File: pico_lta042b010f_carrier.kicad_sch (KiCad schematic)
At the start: 23 parts, among them J1 LTA042B010F_FFC36, J2 5V INPUT, J3 13V8 OUT, U1 RaspberryPi_Pico_2W, U3 MC34063AD

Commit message: chore(kicad): checkpoint before PCB artwork
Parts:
- C11: value 10u 25V -> 10uF 50V; AkizukiCode (none) -> 117897; MPN (none) -> 50PX10MEFC5X11; Manufacturer (none) -> Rubycon; SelectionNote (none) -> 10uF 50V 105C; radial through-hole; positive terminal to GND; SourceURL (none) -> https://akizukidenshi.com/catalog/g/g117897/; Supplier (none) -> Akizuki Denshi
- C6: value 220u 16V -> 220uF 35V; footprint Capacitor_THT:CP_Radial_D5.0mm_P2.00mm -> Capacitor_THT:CP_Radial_D8.0mm_P3.50mm; AkizukiCode (none) -> 111758; MPN (none) -> 35ZLH220MEFCCT8X11.5; Manufacturer (none) -> Rubycon; SelectionNote (none) -> 220uF 35V; linked item sold out; current equivalent candida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; SourceURL (none) -> https://akizukidenshi.com/catalog/g/g111758/; Supplier (none) -> Akizuki Denshi
- C7: value 470p -> 470pF 50V C0G; footprint Capacitor_SMD:C_0805_2012Metric -> Capacitor_THT:C_Disc_D5.0mm_W2.5mm_P2.50mm; AkizukiCode (none) -> 131236; MPN (none) -> RDE5C1H471J0P1H03B; Manufacturer (none) -> Murata; SelectionNote (none) -> 470pF 50V C0G +/-5%; radial through-hole; 2.5mm pitch; SourceURL (none) -> https://akizukidenshi.com/catalog/g/g131236/; Supplier (none) -> Akizuki Denshi
- C8: value 47u 25V -> 47uF 35V; AkizukiCode (none) -> 117887; MPN (none) -> 35PX47MEFC5X11; Manufacturer (none) -> Rubycon; SelectionNote (none) -> 47uF 35V; radial through-hole; SourceURL (none) -> https://akizukidenshi.com/catalog/g/g117887/; Supplier (none) -> Akizuki Denshi
- C9: value 10u 25V -> 10uF 50V; AkizukiCode (none) -> 117897; MPN (none) -> 50PX10MEFC5X11; Manufacturer (none) -> Rubycon; SelectionNote (none) -> 10uF 50V 105C; radial through-hole; SourceURL (none) -> https://akizukidenshi.com/catalog/g/g117897/; Supplier (none) -> Akizuki Denshi
- D4, D6, D7: footprint Diode_SMD:D_SMA -> Diode_THT:D_DO-41_SOD81_P10.16mm_Horizontal; AkizukiCode (none) -> 117244; MPN (none) -> 1N5819; Manufacturer (none) -> WUXI XUYANG ELECTRONICS; SelectionNote (none) -> 40V 1A Schottky; DO-41 through-hole; SourceURL (none) -> https://akizukidenshi.com/catalog/g/g117244/; Supplier (none) -> Akizuki Denshi
- D5: AkizukiCode (none) -> 106423; MPN (none) -> OSG50805C1C; Manufacturer (none) -> OptoSupply; SelectionNote (none) -> green LED; 2012/0805 SMD; hand-solderable; SourceURL (none) -> https://akizukidenshi.com/catalog/g/g106423/; Supplier (none) -> Akizuki Denshi
- D8: AkizukiCode (none) -> 106419; MPN (none) -> OSR50805C1C; Manufacturer (none) -> OptoSupply; SelectionNote (none) -> red LED; 2012/0805 SMD; hand-solderable; SourceURL (none) -> https://akizukidenshi.com/catalog/g/g106419/; Supplier (none) -> Akizuki Denshi
- J2, J3: AkizukiCode (none) -> 108593; MPN (none) -> PH-1X2SG; Manufacturer (none) -> Chang Enn; SelectionNote (none) -> straight 1x2 2.54mm pin header; through-hole; SourceURL (none) -> https://akizukidenshi.com/catalog/g/g108593/; Supplier (none) -> Akizuki Denshi
- L1: value 150uH -> 100uH; footprint Inductor_SMD:L_Sunlord_MWSA1204S-150 -> Inductor_SMD:L_Taiyo-Yuden_NR-10050_9.8x10.0mm_HandSoldering; AkizukiCode (none) -> 108325; MPN (none) -> NR10050T101M; Manufacturer (none) -> Taiyo Yuden; SelectionNote (none) -> 100uH; hand-solder footprint; linked product; SourceURL (none) -> https://akizukidenshi.com/catalog/g/g108325/; Supplier (none) -> Akizuki Denshi
- R10: AkizukiCode (none) -> 111796; MPN (none) -> RG2012N-102-B-T5; Manufacturer (none) -> SUSUMU / SSM; SelectionNote (none) -> 1kohm +/-0.1%; 1/8W; 0805/2012 SMD; hand-solderable; SourceURL (none) -> https://akizukidenshi.com/catalog/g/g111796/; Supplier (none) -> Akizuki Denshi
- R11, R16, R9: AkizukiCode (none) -> 111797; MPN (none) -> RG2012-N-103-B-T5; Manufacturer (none) -> SUSUMU / SSM; SelectionNote (none) -> 10kohm +/-0.1%; 1/8W; 0805/2012 SMD; hand-solderable; SourceURL (none) -> https://akizukidenshi.com/catalog/g/g111797/; Supplier (none) -> Akizuki Denshi
- R7: footprint Resistor_SMD:R_2512_6332Metric_Pad1.40x3.35mm_HandSolder -> Resistor_THT:R_Axial_DIN0207_L6.3mm_D2.5mm_P10.16mm_Horizontal; AkizukiCode (none) -> 108800; MPN (none) -> MFU100F0R47B; Manufacturer (none) -> FAITHFUL LINK INDUSTRIAL CORP.; SelectionNote (none) -> 0.47ohm +/-1%; 1W; axial through-hole; hand-solder; SourceURL (none) -> https://akizukidenshi.com/catalog/g/g108800/; Supplier (none) -> Akizuki Denshi
- R8: footprint Resistor_SMD:R_0805_2012Metric -> Resistor_SMD:R_0603_1608Metric; AkizukiCode (none) -> 131855; MPN (none) -> RC0603J200R; Manufacturer (none) -> FAITHFUL LINK INDUSTRIAL CORP.; SelectionNote (none) -> 200ohm +/-5%; 0.1W; 0603/1608 SMD; hand-solderable; SourceURL (none) -> https://akizukidenshi.com/catalog/g/g131855/; Supplier (none) -> Akizuki Denshi
- RV1: AkizukiCode (none) -> 100975; MPN (none) -> 3296W-1-103LF; Manufacturer (none) -> Bourns; SelectionNote (none) -> 10kohm vertical multiturn trimmer; through-hole; SourceURL (none) -> https://akizukidenshi.com/catalog/g/g100975/; Supplier (none) -> Akizuki Denshi
- U1: AkizukiCode (none) -> 130330; MPN (none) -> SC1633; Manufacturer (none) -> Raspberry Pi Foundation; SelectionNote (none) -> Raspberry Pi Pico 2 W module; SourceURL (none) -> https://akizukidenshi.com/catalog/g/g130330/; Supplier (none) -> Akizuki Denshi
- U3: AkizukiCode (none) -> 117573; MPN (none) -> MC34063AD; Manufacturer (none) -> TAEJIN TECHNOLOGY; SelectionNote (none) -> SOP-8; hand-solderable 1.27mm pitch; SourceURL (none) -> https://akizukidenshi.com/catalog/g/g117573/; Supplier (none) -> Akizuki Denshi

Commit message: Update hand-solder components and preserve current PCB layout
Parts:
- R10: value 1k 1% -> 1k 0.1%; footprint Resistor_SMD:R_0805_2012Metric -> Resistor_THT:R_Axial_DIN0207_L6.3mm_D2.5mm_P10.16mm_Horizontal; AkizukiCode 111796 -> 116876; MPN RG2012N-102-B-T5 -> MF25B1KBD; Manufacturer SUSUMU / SSM -> FAITHFUL LINK INDUSTRIAL CORP.; SelectionNote 1kohm +/-0.1%; 1/8W; 0805/2012 SMD; hand-solderable -> 1kohm +/-0.1%; 1/4W; axial through-hole; horizontal mounting; SourceURL https://akizukidenshi.com/catalog/g/g111796/ -> https://akizukidenshi.com/catalog/g/g116876/
- R11, R16, R9: value 10k 1% -> 10k 0.1%; footprint Resistor_SMD:R_0805_2012Metric -> Resistor_THT:R_Axial_DIN0207_L6.3mm_D2.5mm_P10.16mm_Horizontal; AkizukiCode 111797 -> 116877; MPN RG2012-N-103-B-T5 -> MF25B10KBD; Manufacturer SUSUMU / SSM -> FAITHFUL LINK INDUSTRIAL CORP.; SelectionNote 10kohm +/-0.1%; 1/8W; 0805/2012 SMD; hand-solderable -> 10kohm +/-0.1%; 1/4W; axial through-hole; horizontal mounti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; SourceURL https://akizukidenshi.com/catalog/g/g111797/ -> https://akizukidenshi.com/catalog/g/g116877/
- R8: value 200 -> 200 1%; footprint Resistor_SMD:R_0603_1608Metric -> Resistor_THT:R_Axial_DIN0204_L3.6mm_D1.6mm_P5.08mm_Horizontal; AkizukiCode 131855 -> 108526; MPN RC0603J200R -> MFS25F200RB; SelectionNote 200ohm +/-5%; 0.1W; 0603/1608 SMD; hand-solderable -> 200ohm +/-1%; 1/4W; compact axial through-hole; horizontal 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; SourceURL https://akizukidenshi.com/catalog/g/g131855/ -> https://akizukidenshi.com/catalog/g/g108526/
- RV1: footprint Potentiometer_THT:Potentiometer_Bourns_3296W_Vertical -> Potentiometer_THT:Potentiometer_Runtron_RM-065_Vertical; AkizukiCode 100975 -> 106063; MPN 3296W-1-103LF -> TSR-065-103-R; Manufacturer Bourns -> SUNTAN TECHNOLOGY CO LTD; SelectionNote 10kohm vertical multiturn trimmer; through-hole -> 10kohm +/-30%; 0.1W; top-adjust single-turn trimmer; RM-065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; SourceURL https://akizukidenshi.com/catalog/g/g100975/ -> https://akizukidenshi.com/catalog/g/g106063/

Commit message: Update power-stage layout and component selections
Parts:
- D5: value GREEN LED -> GREEN LED 3mm; footprint LED_SMD:LED_0805_2012Metric -> LED_THT:LED_D3.0mm; AkizukiCode 106423 -> 111635; MPN OSG50805C1C -> OSG5TA3Z74A; SelectionNote green LED; 2012/0805 SMD; hand-solderable -> green 3mm bullet LED; radial through-hole; 2.54mm pitch; SourceURL https://akizukidenshi.com/catalog/g/g106423/ -> https://akizukidenshi.com/catalog/g/g111635/
- D8: value RED LED -> RED LED 3mm; footprint LED_SMD:LED_0805_2012Metric -> LED_THT:LED_D3.0mm; AkizukiCode 106419 -> 111577; MPN OSR50805C1C -> OSR5JA3Z74A; SelectionNote red LED; 2012/0805 SMD; hand-solderable -> red 3mm bullet LED; radial through-hole; 2.54mm pitch; SourceURL https://akizukidenshi.com/catalog/g/g106419/ -> https://akizukidenshi.com/catalog/g/g111577/
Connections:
- net +13V8: no longer C9.1
- net SW_NODE: now also C9.1
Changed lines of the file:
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@@
 		(exclude_from_sim no) (in_bom yes) (on_board yes) (dnp no)
 		(property "Reference" "D5" (at 169.04 42.04 270) (effects (font (size 1.27 1.27))))
-		(property "Value" "GREEN LED" (at 173.99 47.04 270) (effects (font (size 1.27 1.27))))
-		(property "Footprint" "LED_SMD:LED_0805_2012Metric" (at 0 0 0) (effects (font (size 1.27 1.27)) hide))		(property "Manufacturer" "OptoSupply" (at 0 0 0) (effects (font (size 1.27 1.27)) hide))
-		(property "MPN" "OSG50805C1C" (at 0 0 0) (effects (font (size 1.27 1.27)) hide))
-		(property "AkizukiCode" "106423" (at 0 0 0) (effects (font (size 1.27 1.27)) hide))
+		(property "Value" "GREEN LED 3mm" (at 173.99 47.04 270) (effects (font (size 1.27 1.27))))
+		(property "Footprint" "LED_THT:LED_D3.0mm" (at 0 0 0) (effects (font (size 1.27 1.27)) hide))		(property "Manufacturer" "OptoSupply" (at 0 0 0) (effects (font (size 1.27 1.27)) hide))
+		(property "MPN" "OSG5TA3Z74A" (at 0 0 0) (effects (font (size 1.27 1.27)) hide))
+		(property "AkizukiCode" "111635" (at 0 0 0) (effects (font (size 1.27 1.27)) hide))
 		(property "Supplier" "Akizuki Denshi" (at 0 0 0) (effects (font (size 1.27 1.27)) hide))
-		(property "SourceURL" "https://akizukidenshi.com/catalog/g/g106423/" (at 0 0 0) (effects (font (size 1.27 1.27)) hide))
-		(property "SelectionNote" "green LED; 2012/0805 SMD; hand-solderable" (at 0 0 0) (effects (font (size 1.27 1.27)) hide))
+		(property "SourceURL" "https://akizukidenshi.com/catalog/g/g111635/" (at 0 0 0) (effects (font (size 1.27 1.27)) hide))
+		(property "SelectionNote" "green 3mm bullet LED; radial through-hole; 2.54mm pitch" (at 0 0 0) (effects (font (size 1.27 1.27)) hide))
 		(pin "1")
 		(pin "2")
@@
 		(exclude_from_sim no) (in_bom yes) (on_board yes) (dnp no)
 		(property "Reference" "D8" (at 231.04 50.8 90) (effects (font (size 1.27 1.27))))
-		(property "Value" "RED LED" (at 231.04 55.88 90) (effects (font (size 1.27 1.27))))
-		(property "Footprint" "LED_SMD:LED_0805_2012Metric" (at 0 0 0) (effects (font (size 1.27 1.27)) hide))		(property "Manufacturer" "OptoSupply" (at 0 0 0) (effects (font (size 1.27 1.27)) hide))
-		(property "MPN" "OSR50805C1C" (at 0 0 0) (effects (font (size 1.27 1.27)) hide))
-		(property "AkizukiCode" "106419" (at 0 0 0) (effects (font (size 1.27 1.27)) hide))
+		(property "Value" "RED LED 3mm" (at 231.04 55.88 90) (effects (font (size 1.27 1.27))))
+		(property "Footprint" "LED_THT:LED_D3.0mm" (at 0 0 0) (effects (font (size 1.27 1.27)) hide))		(property "Manufacturer" "OptoSupply" (at 0 0 0) (effects (font (size 1.27 1.27)) hide))
+		(property "MPN" "OSR5JA3Z74A" (at 0 0 0) (effects (font (size 1.27 1.27)) hide))
+		(property "AkizukiCode" "111577" (at 0 0 0) (effects (font (size 1.27 1.27)) hide))
 		(property "Supplier" "Akizuki Denshi" (at 0 0 0) (effects (font (size 1.27 1.27)) hide))
-		(property "SourceURL" "https://akizukidenshi.com/catalog/g/g106419/" (at 0 0 0) (effects (font (size 1.27 1.27)) hide))
-		(property "SelectionNote" "red LED; 2012/0805 SMD; hand-solderable" (at 0 0 0) (effects (font (size 1.27 1.27)) hide))
+		(property "SourceURL" "https://akizukidenshi.com/catalog/g/g111577/" (at 0 0 0) (effects (font (size 1.27 1.27)) hide))
+		(property "SelectionNote" "red 3mm bullet LED; radial through-hole; 2.54mm pitch" (at 0 0 0) (effects (font (size 1.27 1.27)) hide))
 		(pin "1")
 		(pin "2")
@@
 	(wire
 		(pts
-			(xy 123.19 21.59) (xy 181.61 21.59)
+				(xy 123.19 21.59) (xy 163.83 21.59)
 		)
 		(stroke (width 0) (type solid))
@@
 	(wire
 		(pts
-			(xy 181.61 31.75) (xy 181.61 21.59)
+				(xy 111.76 21.59) (xy 111.76 15.24)
+		)
+		(stroke (width 0) (type solid))
+	)
+	(wire
+		(pts
+				(xy 111.76 15.24) (xy 181.61 15.24)
+		)
+		(stroke (width 0) (type solid))
+	)
+	(wire
+		(pts
+				(xy 181.61 15.24) (xy 181.61 31.75)
 		)
 		(stroke (width 0) (type solid))
@@
 	(junction
 		(at 66.04 35.56)
+		(diameter 1.016)
+		(color 0 0 0 0)
+	)
+	(junction
+		(at 111.76 21.59)
 		(diameter 1.016)
 		(color 0 0 0 0)
@@
 		(effects (font (size 0.01 0.01)) (hide yes))
 	)
-	(label "+13V8"
+	(label "SW_NODE"
 		(at 181.61 31.75 0)
 		(effects (font (size 0.01 0.01)) (hide yes))

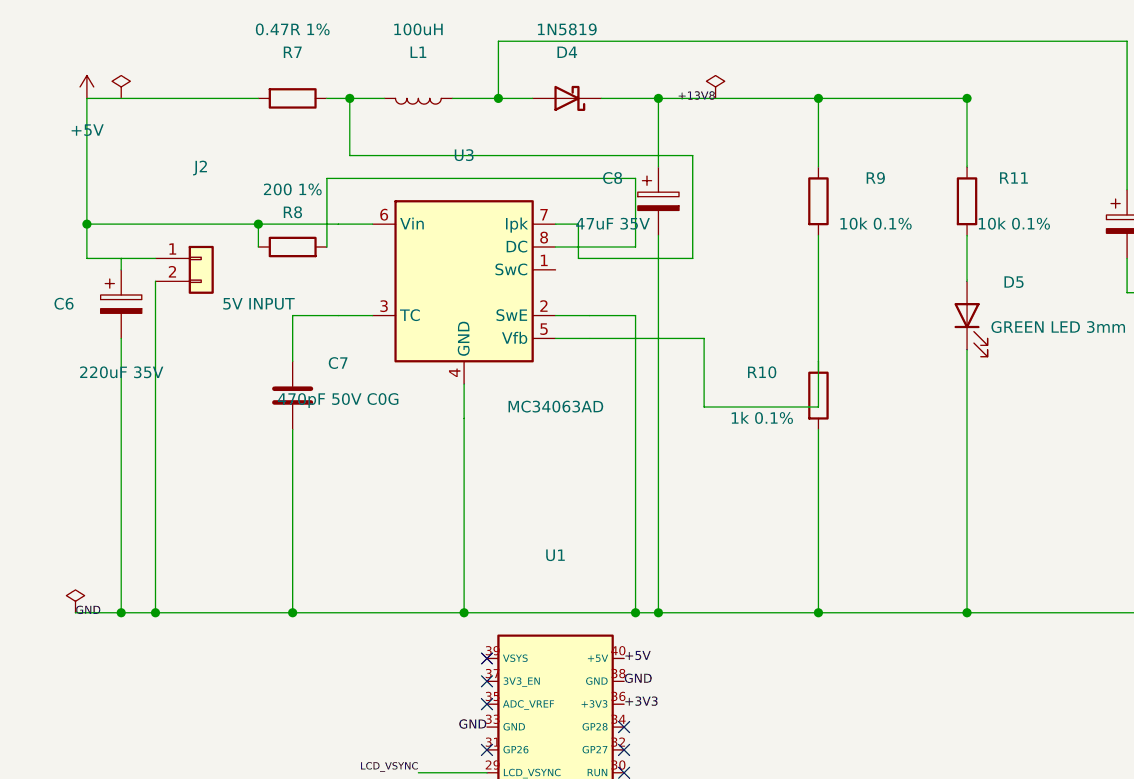
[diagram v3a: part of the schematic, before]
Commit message: Update power stage for vertical parts and USB-C input
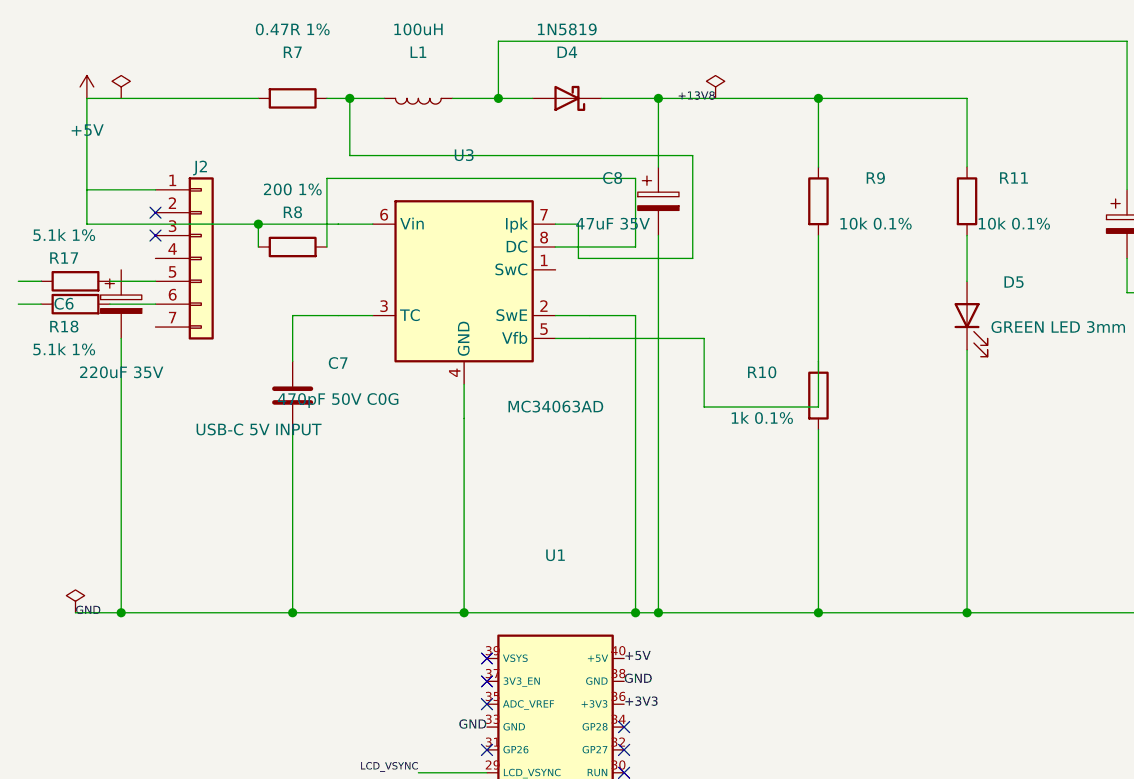
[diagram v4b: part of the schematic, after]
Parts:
- added R17, R18: 5.1k 1%, Resistor_THT:R_Axial_DIN0204_L3.6mm_D1.6mm_P2.54mm_Vertical, symbol Device:R
- D4, D6, D7: footprint Diode_THT:D_DO-41_SOD81_P10.16mm_Horizontal -> Diode_THT:D_DO-41_SOD81_P2.54mm_Vertical_KathodeUp; SelectionNote 40V 1A Schottky; DO-41 through-hole -> 40V 1A Schottky; DO-41 through-hole; vertical mounting
- J2: value 5V INPUT -> USB-C 5V INPUT; footprint Connector_PinHeader_2.54mm:PinHeader_1x02_P2.54mm_Vertical -> Custom:AE_USB2.0_TYPE_C; symbol Connector_Generic:Conn_01x02 -> Connector_Generic:Conn_01x07; AkizukiCode 108593 -> 113080; MPN PH-1X2SG -> AE-USB2.0-TYPE-C; Manufacturer Chang Enn -> Akizuki Denshi Tsusho; SelectionNote straight 1x2 2.54mm pin header; through-hole -> USB Type-C female breakout; seven 2.54mm through-hole pins;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; SourceURL https://akizukidenshi.com/catalog/g/g108593/ -> https://akizukidenshi.com/catalog/g/g113080/
- R10: footprint Resistor_THT:R_Axial_DIN0207_L6.3mm_D2.5mm_P10.16mm_Horizontal -> Resistor_THT:R_Axial_DIN0207_L6.3mm_D2.5mm_P2.54mm_Vertical; SelectionNote 1kohm +/-0.1%; 1/4W; axial through-hole; horizontal mounting -> 1kohm +/-0.1%; 1/4W; axial through-hole; vertical mounting
- R11, R16, R9: footprint Resistor_THT:R_Axial_DIN0207_L6.3mm_D2.5mm_P10.16mm_Horizontal -> Resistor_THT:R_Axial_DIN0207_L6.3mm_D2.5mm_P2.54mm_Vertical; SelectionNote 10kohm +/-0.1%; 1/4W; axial through-hole; horizontal mounti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 -> 10kohm +/-0.1%; 1/4W; axial through-hole; vertical mounting
- R7: footprint Resistor_THT:R_Axial_DIN0207_L6.3mm_D2.5mm_P10.16mm_Horizontal -> Resistor_THT:R_Axial_DIN0411_L9.9mm_D3.6mm_P5.08mm_Vertical; SelectionNote 0.47ohm +/-1%; 1W; axial through-hole; hand-solder -> 0.47ohm +/-1%; 1W; axial through-hole; vertical mounting
- R8: footprint Resistor_THT:R_Axial_DIN0204_L3.6mm_D1.6mm_P5.08mm_Horizontal -> Resistor_THT:R_Axial_DIN0204_L3.6mm_D1.6mm_P2.54mm_Vertical; SelectionNote 200ohm +/-1%; 1/4W; compact axial through-hole; horizontal 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 -> 200ohm +/-1%; 1/4W; compact axial through-hole; vertical mo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
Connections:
- net GND: now also J2.4 (Pin_4), J2.7 (Pin_7), R17.1, R18.1; no longer J2.2 (Pin_2)
- new net USB_CC1: J2.5 (Pin_5), R17.2
- new net USB_CC2: J2.6 (Pin_6), R18.2
- no-connect marks 9 -> 11
